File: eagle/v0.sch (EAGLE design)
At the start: 50 parts, among them IC1 MCP23008/SO, J12 455-1750-1-ND, J13 455-1750-1-ND, J14 455-1750-1-ND, J15 455-1750-1-ND, Q1 IRLML6244, Q2 IRLML6244, Q3 IRLML6244, Q4 IRLML6244, Q5 IRLML6244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

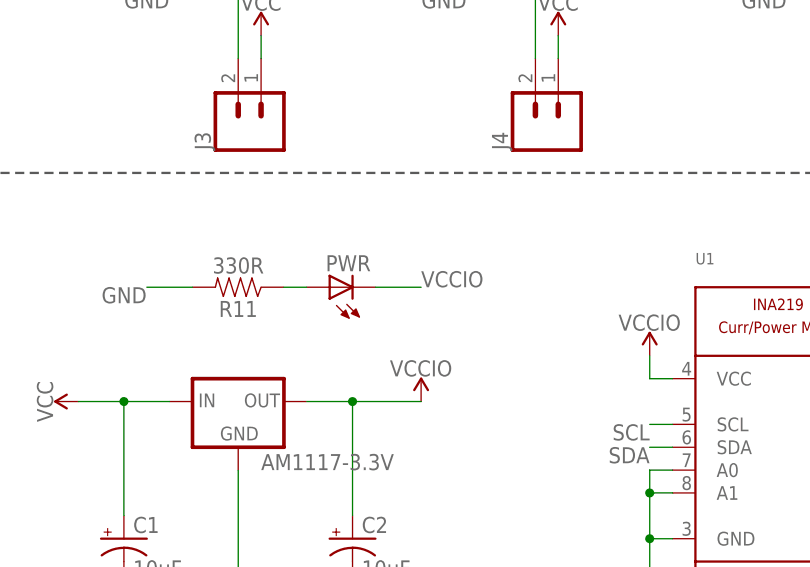
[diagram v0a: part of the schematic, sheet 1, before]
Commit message: Fix LED polarity - caught by my dad :)
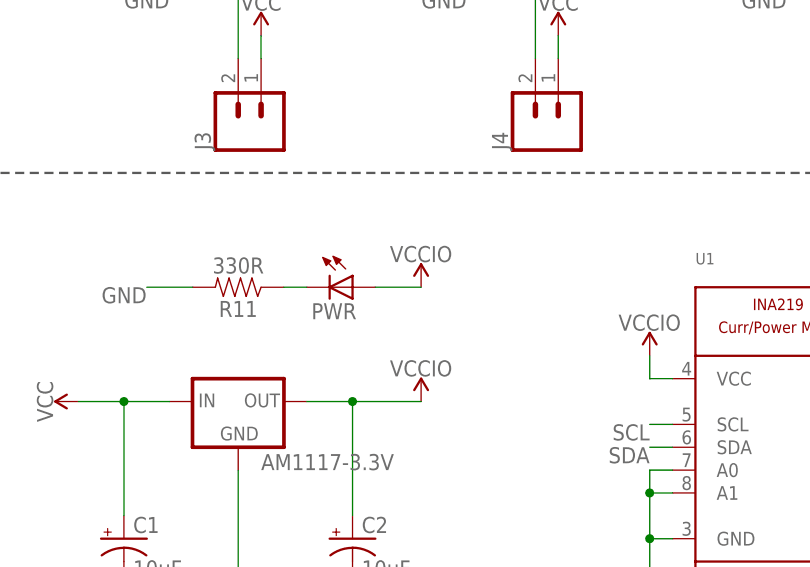
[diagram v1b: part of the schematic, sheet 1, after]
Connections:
- net N$17: now also PWR.C; no longer PWR.A
- net VCCIO: now also PWR.A; no longer PWR.C
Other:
- moved on the sheet: PWR
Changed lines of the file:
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@@
 <part name="FRAME1" library="SparkFun-Aesthetics" deviceset="FRAME-A4L" device=""/>
 <part name="FRAME2" library="SparkFun-Aesthetics" deviceset="FRAME-A4L" device=""/>
+<part name="SUPPLY9" library="SparkFun-PowerSymbols" deviceset="VCCIO" device=""/>
 </parts>
 <sheets>
@@
 <attribute name="VALUE" x="76.2" y="84.074" size="1.778" layer="96" align="bottom-center"/>
 </instance>
-<instance part="PWR" gate="G$1" x="66.04" y="93.98" smashed="yes" rot="R90">
-<attribute name="NAME" x="70.612" y="97.536" size="1.778" layer="95" rot="R180"/>
-<attribute name="VALUE" x="70.612" y="99.695" size="1.778" layer="96" rot="R180"/>
+<instance part="PWR" gate="G$1" x="68.58" y="93.98" smashed="yes" rot="R270">
+<attribute name="NAME" x="64.008" y="90.424" size="1.778" layer="95"/>
+<attribute name="VALUE" x="64.008" y="88.265" size="1.778" layer="96"/>
 </instance>
 <instance part="R11" gate="G$1" x="55.88" y="93.98" smashed="yes" rot="R180">
@@
 <attribute name="SHEET" x="195.58" y="1.27" size="2.54" layer="94" font="vector"/>
 <attribute name="DESIGNER" x="226.26" y="6.35" size="2.54" layer="94" font="vector"/>
+</instance>
+<instance part="SUPPLY9" gate="G$1" x="76.2" y="93.98" smashed="yes">
+<attribute name="VALUE" x="76.2" y="96.774" size="1.778" layer="96" align="bottom-center"/>
 </instance>
 </instances>
@@
 </segment>
 <segment>
-<pinref part="PWR" gate="G$1" pin="C"/>
-<wire x1="71.12" y1="93.98" x2="76.2" y2="93.98" width="0.1524" layer="91"/>
-<label x="76.2" y="93.98" size="1.778" layer="95"/>
-</segment>
-<segment>
 <pinref part="U1" gate="G$1" pin="VCC"/>
 <wire x1="104.14" y1="83.82" x2="101.6" y2="83.82" width="0.1524" layer="91"/>
@@
 <pinref part="SUPPLY15" gate="G$1" pin="VCCIO"/>
 </segment>
+<segment>
+<pinref part="PWR" gate="G$1" pin="A"/>
+<wire x1="71.12" y1="93.98" x2="76.2" y2="93.98" width="0.1524" layer="91"/>
+<pinref part="SUPPLY9" gate="G$1" pin="VCCIO"/>
+</segment>
 </net>
 <net name="SDA" class="0">
@@
 <wire x1="104.14" y1="78.74" x2="101.6" y2="78.74" width="0.1524" layer="91"/>
 <label x="101.6" y="78.74" size="1.778" layer="95" rot="R180"/>
-</segment>
-</net>
-<net name="N$17" class="0">
-<segment>
-<pinref part="PWR" gate="G$1" pin="A"/>
-<pinref part="R11" gate="G$1" pin="1"/>
-<wire x1="63.5" y1="93.98" x2="60.96" y2="93.98" width="0.1524" layer="91"/>
 </segment>
 </net>
@@
 </segment>
 </net>
+<net name="N$17" class="0">
+<segment>
+<pinref part="R11" gate="G$1" pin="1"/>
+<pinref part="PWR" gate="G$1" pin="C"/>
+<wire x1="63.5" y1="93.98" x2="60.96" y2="93.98" width="0.1524" layer="91"/>
+</segment>
+</net>
